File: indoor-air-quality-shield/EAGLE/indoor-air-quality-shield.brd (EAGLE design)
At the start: 105.4 x 38.1 mm, 43 parts, among them IC1 LM358D, IC2 LM358D, Q1 MMBT2222A, Q2 MMBT2222A, Q3 MMBT2222A

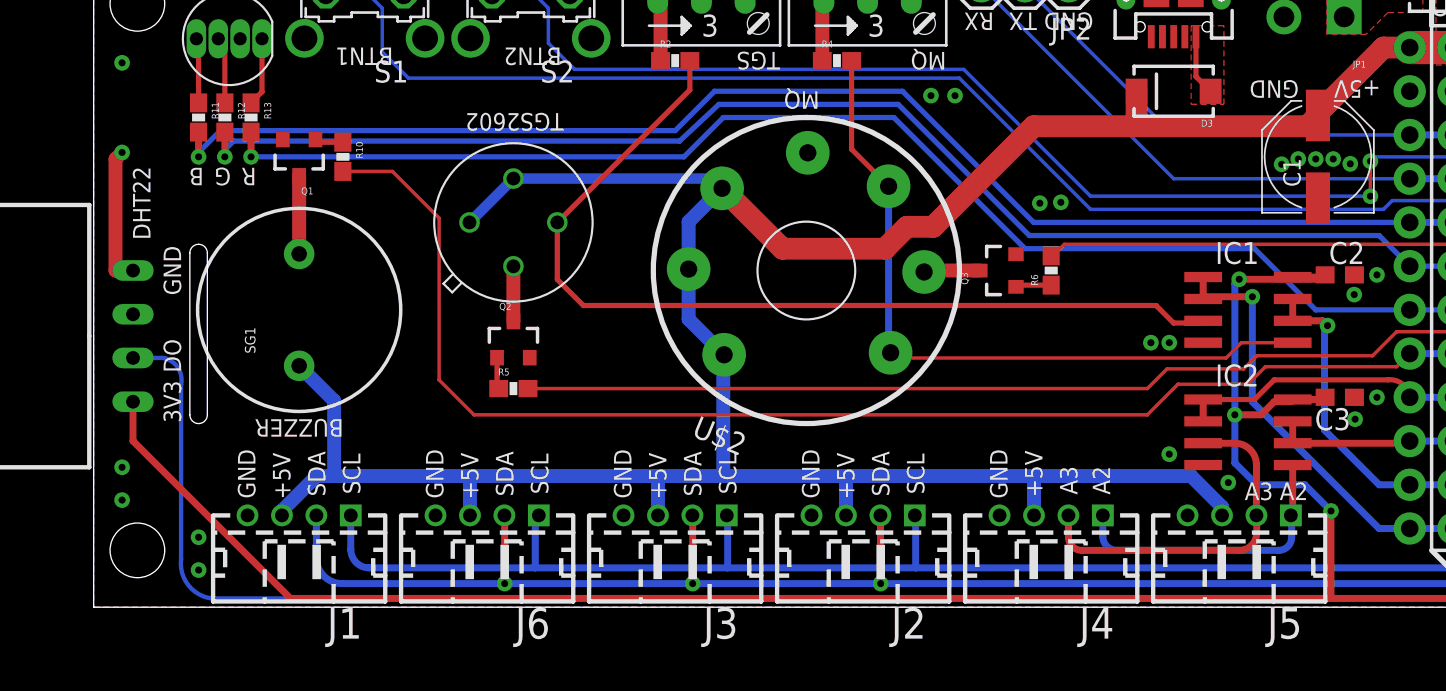
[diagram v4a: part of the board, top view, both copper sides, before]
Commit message: added bypass caps and labeled connectors
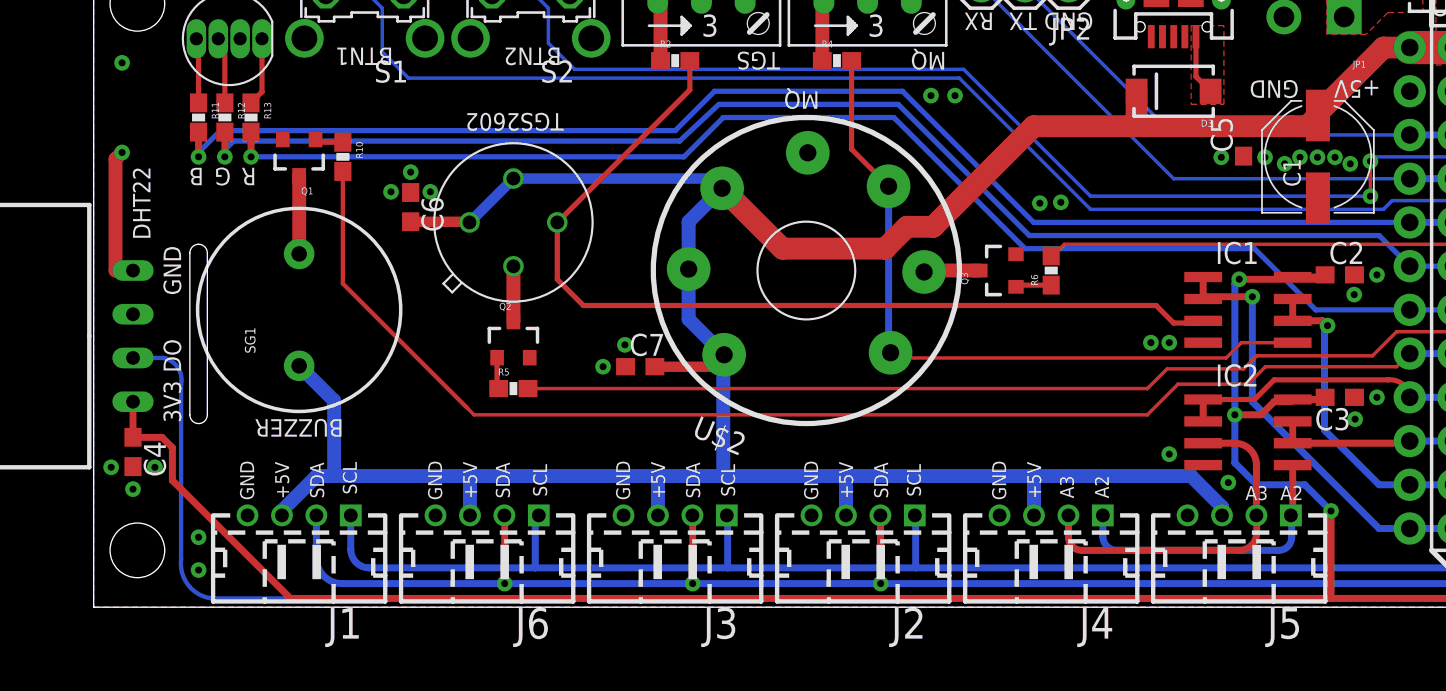
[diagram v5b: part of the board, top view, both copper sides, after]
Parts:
- added C4, C5, C6, C7: (no value), rcl:C0603
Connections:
- net +3V3: now also C4.1
- net +5V: now also C5.2, C6.2, C7.2
- net GND: now also C4.2, C5.1, C6.1, C7.1
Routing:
- net +5V: track 192.2 -> 202.8 mm
- net BUZZER: track 79.9 -> 78.2 mm
- net +3V3: track 169.0 -> 170.0 mm
- net GND: vias 26 -> 34
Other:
- board text added: "1"
- board text added: "2"
- board text added: "3"
- board text added: "4"
- board text added: "5"
- board text added: "6"
